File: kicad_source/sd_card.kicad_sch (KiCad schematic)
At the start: 7 parts, among them J1 Conn_01x08

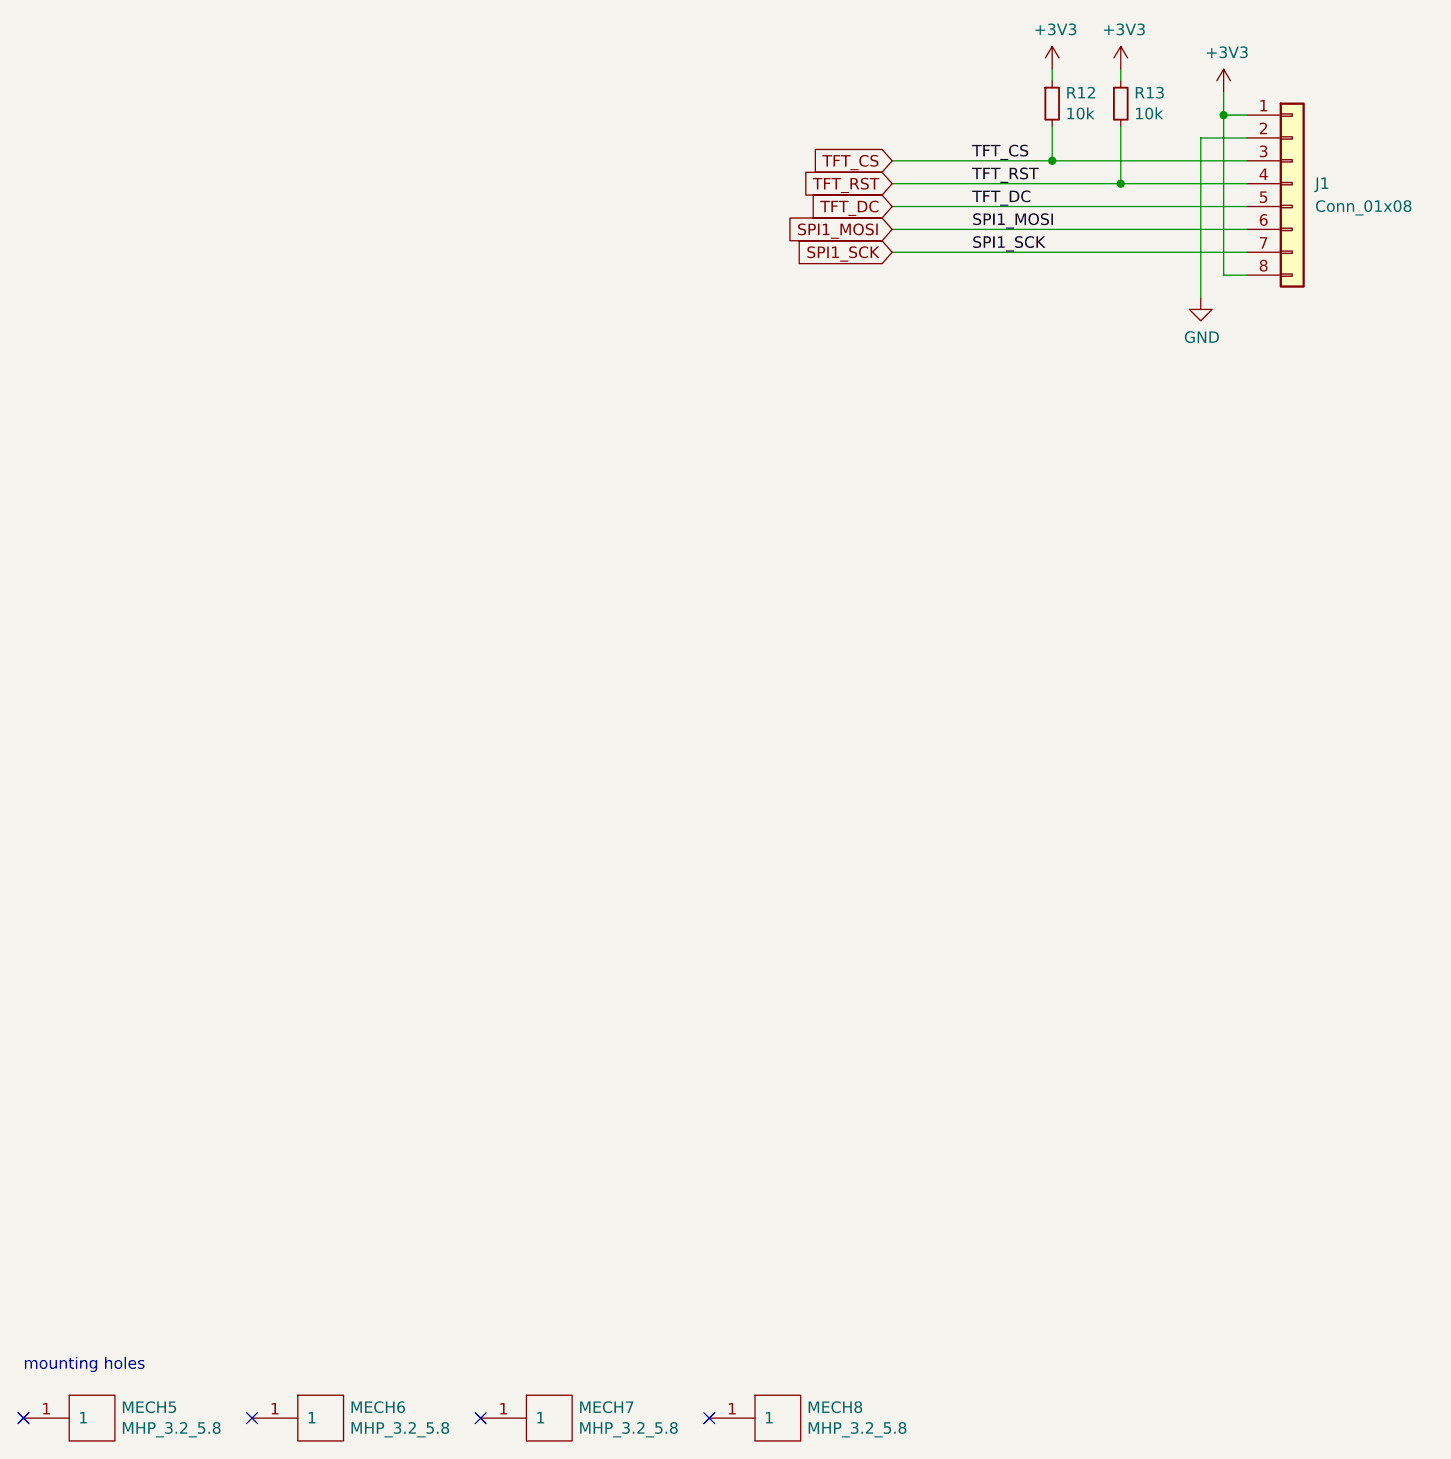
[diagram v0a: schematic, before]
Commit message: added sd card, updated layout
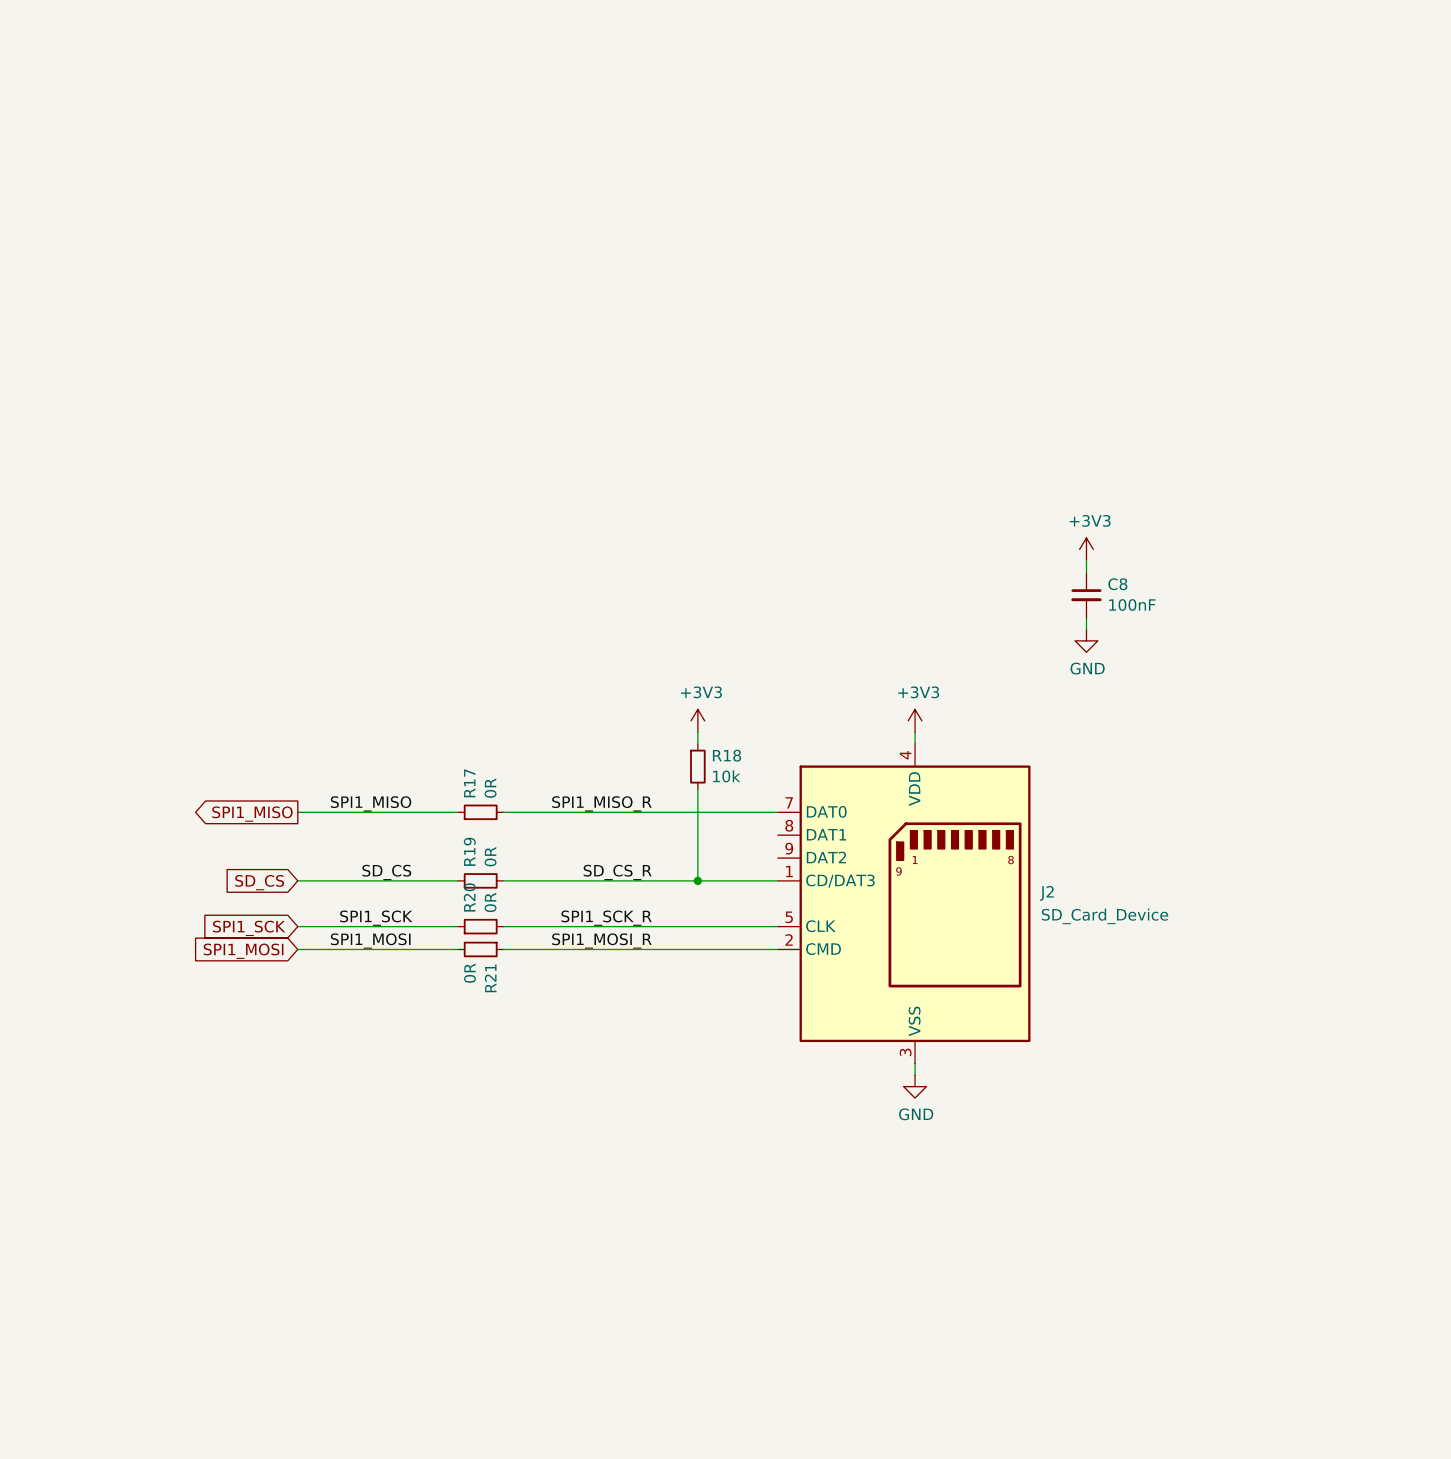
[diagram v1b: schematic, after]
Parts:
- removed J1: Conn_01x08, Connector_PinHeader_2.54mm:PinHeader_1x08_P2.54mm_Vertical, symbol Connector_Generic:Conn_01x08
- removed MECH5, MECH6, MECH7, MECH8: MHP_3.2_5.8, MountingHole:MountingHole_3.2mm_M3_ISO14580_Pad, symbol OpenCyphalPicoBase-rescue:MHP_3.2_5.8-MECH_mounting-holes
- removed R12, R13: 10k, Resistor_SMD:R_0603_1608Metric, symbol Device:R_Small
- added C8: 100nF, Capacitor_SMD:C_0603_1608Metric, symbol Device:C_Small
- added J2: SD_Card_Device, Connector_Card:microSD_HC_Molex_104031-0811, symbol Connector:SD_Card_Device
- added R17, R19, R20, R21: 0R, Resistor_SMD:R_0603_1608Metric, symbol Device:R_Small
- added R18: 10k, Resistor_SMD:R_0603_1608Metric, symbol Device:R_Small
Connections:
- net +3V3: now also C8.1, J2.4 (VDD), R18.1
- net GND: now also C8.2, J2.3 (VSS), J2.6 (VSS)
- net SPI1_MOSI: now also R21.2
- net SPI1_SCK: now also R20.1
- new net SD_CS: R19.1
- new net SD_CS_R: J2.1 (CD/DAT3), R18.2, R19.2
- new net SPI1_MISO: R17.1
- new net SPI1_MISO_R: J2.7 (DAT0), R17.2
- new net SPI1_MOSI_R: J2.2 (CMD), R21.1
- new net SPI1_SCK_R: J2.5 (CLK), R20.2
- no-connect marks 4 -> 0
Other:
- note removed: "mounting holes"

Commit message: added push button
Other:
- title: CyphalIMUBase/CAN -> CyphalHMIBase/CAN
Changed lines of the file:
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@@
 	(paper "A4")
 	(title_block
-		(title "CyphalIMUBase/CAN")
+		(title "CyphalHMIBase/CAN")
 		(date "2026-06-05")
 		(rev "0.1")
@@
 				(justify right)
 				(hide yes)
+			)
+		)
+	)
+	(symbol
+		(lib_id "OpenCyphalPicoBase-rescue:+3.3V-power-supply")
+		(at 133.35 111.76 0)
+		(unit 1)
+		(exclude_from_sim no)
+		(in_bom yes)
+		(on_board yes)
+		(dnp no)
+		(property "Reference" "#PWR53"
+			(at 133.35 115.57 0)
+			(effects
+				(font
+					(size 1.27 1.27)
+				)
+				(hide yes)
+			)
+		)
+		(property "Value" "+3V3"
+			(at 133.731 107.3658 0)
+			(effects
+				(font
+					(size 1.27 1.27)
+				)
+			)
+		)
+		(property "Footprint" ""
+			(at 133.35 111.76 0)
+			(effects
+				(font
+					(size 1.27 1.27)
+				)
+			)
+		)
+		(property "Datasheet" ""
+			(at 133.35 111.76 0)
+			(effects
+				(font
+					(size 1.27 1.27)
+				)
+			)
+		)
+		(property "Description" ""
+			(at 133.35 111.76 0)
+			(effects
+				(font
+					(size 1.27 1.27)
+				)
+				(hide yes)
+			)
+		)
+		(pin "1"
+		)
+		(instances
+			(project "CyphalHMIBase-CAN"
+				(path "/9d6d512e-1439-4aa2-b0d9-afb2dddd9146/e75f9fc4-b9ac-41b4-8a83-2ca859e56dc6"
+					(reference "#PWR53")
+					(unit 1)
+				)
 			)
 		)
@@
 	(symbol
 		(lib_id "OpenCyphalPicoBase-rescue:GND-power-supply")
+		(at 133.35 149.86 0)
+		(unit 1)
+		(exclude_from_sim no)
+		(in_bom yes)
+		(on_board yes)
+		(dnp no)
+		(property "Reference" "#PWR55"
+			(at 133.35 156.21 0)
+			(effects
+				(font
+					(size 1.27 1.27)
+				)
+				(hide yes)
+			)
+		)
+		(property "Value" "GND"
+			(at 133.477 154.2542 0)
+			(effects
+				(font
+					(size 1.27 1.27)
+				)
+			)
+		)
+		(property "Footprint" ""
+			(at 133.35 149.86 0)
+			(effects
+				(font
+					(size 1.27 1.27)
+				)
+			)
+		)
+		(property "Datasheet" ""
+			(at 133.35 149.86 0)
+			(effects
+				(font
+					(size 1.27 1.27)
+				)
+			)
+		)
+		(property "Description" ""
+			(at 133.35 149.86 0)
+			(effects
+				(font
+					(size 1.27 1.27)
+				)
+				(hide yes)
+			)
+		)
+		(pin "1"
+		)
+		(instances
+			(project "CyphalHMIBase-CAN"
+				(path "/9d6d512e-1439-4aa2-b0d9-afb2dddd9146/e75f9fc4-b9ac-41b4-8a83-2ca859e56dc6"
+					(reference "#PWR55")
+					(unit 1)
+				)
+			)
+		)
+	)
+	(symbol
+		(lib_id "OpenCyphalPicoBase-rescue:GND-power-supply")
 		(at 152.4 100.33 0)
 		(unit 1)
@@
 	(symbol
 		(lib_id "Device:R_Small")
+		(at 85.09 128.27 90)
+		(unit 1)
+		(exclude_from_sim no)
+		(in_bom yes)
+		(on_board yes)
+		(dnp no)
+		(property "Reference" "R19"
+			(at 83.9216 126.7714 0)
+			(effects
+				(font
+					(size 1.27 1.27)
+				)
+				(justify left)
+			)
+		)
+		(property "Value" "0R"
+			(at 86.233 126.7714 0)
+			(effects
+				(font
+					(size 1.27 1.27)
+				)
+				(justify left)
+			)
+		)
+		(property "Footprint" "Resistor_SMD:R_0603_1608Metric"
+			(at 88.9 128.27 0)
+			(effects
+				(font
+					(size 1.27 1.27)
+				)
+				(hide yes)
+			)
+		)
+		(property "Datasheet" ""
+			(at 85.09 128.27 0)
+			(effects
+				(font
+					(size 1.27 1.27)
+				)
+			)
+		)
+		(property "Description" ""
+			(at 85.09 128.27 0)
+			(effects
+				(font
+					(size 1.27 1.27)
+				)
+				(hide yes)
+			)
+		)
+		(property "LCSC" "C22775"
+			(at 85.09 128.27 0)
+			(effects
+				(font
+					(size 1.27 1.27)
+				)
+				(hide yes)
+			)
+		)
+		(pin "1"
+		)
+		(pin "2"
+		)
+		(instances
+			(project "CyphalHMIBase-CAN"
+				(path "/9d6d512e-1439-4aa2-b0d9-afb2dddd9146/e75f9fc4-b9ac-41b4-8a83-2ca859e56dc6"
+					(reference "R19")
+					(unit 1)
+				)
+			)
+		)
+	)
+	(symbol
+		(lib_id "Device:R_Small")
 		(at 109.22 115.57 0)
 		(unit 1)
@@
 				(path "/9d6d512e-1439-4aa2-b0d9-afb2dddd9146/e75f9fc4-b9ac-41b4-8a83-2ca859e56dc6"
 					(reference "R18")
-					(unit 1)
-				)
-			)
-		)
-	)
-	(symbol
-		(lib_id "Device:R_Small")
-		(at 85.09 128.27 90)
-		(unit 1)
-		(exclude_from_sim no)
-		(in_bom yes)
-		(on_board yes)
-		(dnp no)
-		(property "Reference" "R19"
-			(at 83.9216 126.7714 0)
-			(effects
-				(font
-					(size 1.27 1.27)
-				)
-				(justify left)
-			)
-		)
-		(property "Value" "0R"
-			(at 86.233 126.7714 0)
-			(effects
-				(font
-					(size 1.27 1.27)
-				)
-				(justify left)
-			)
-		)
-		(property "Footprint" "Resistor_SMD:R_0603_1608Metric"
-			(at 88.9 128.27 0)
-			(effects
-				(font
-					(size 1.27 1.27)
-				)
-				(hide yes)
-			)
-		)
-		(property "Datasheet" ""
-			(at 85.09 128.27 0)
-			(effects
-				(font
-					(size 1.27 1.27)
-				)
-			)
-		)
-		(property "Description" ""
-			(at 85.09 128.27 0)
-			(effects
-				(font
-					(size 1.27 1.27)
-				)
-				(hide yes)
-			)
-		)
-		(property "LCSC" "C22775"
-			(at 85.09 128.27 0)
-			(effects
-				(font
-					(size 1.27 1.27)
-				)
-				(hide yes)
-			)
-		)
-		(pin "1"
-		)
-		(pin "2"
-		)
-		(instances
-			(project "CyphalHMIBase-CAN"
-				(path "/9d6d512e-1439-4aa2-b0d9-afb2dddd9146/e75f9fc4-b9ac-41b4-8a83-2ca859e56dc6"
-					(reference "R19")
 					(unit 1)
 				)
@@
 					(unit 1)
 				)
-			)
-		)
-	)
-	(symbol
-		(lib_id "OpenCyphalPicoBase-rescue:+3.3V-power-supply")
-		(at 133.35 111.76 0)
-		(unit 1)
-		(exclude_from_sim no)
-		(in_bom yes)
-		(on_board yes)
-		(dnp no)
-		(property "Reference" "#PWR53"
-			(at 133.35 115.57 0)
-			(effects
-				(font
-					(size 1.27 1.27)
-				)
-				(hide yes)
-			)
-		)
-		(property "Value" "+3V3"
-			(at 133.731 107.3658 0)
-			(effects
-				(font
-					(size 1.27 1.27)
-				)
-			)
-		)
-		(property "Footprint" ""
-			(at 133.35 111.76 0)
-			(effects
-				(font
-					(size 1.27 1.27)
-				)
-			)
-		)
-		(property "Datasheet" ""
-			(at 133.35 111.76 0)
-			(effects
-				(font
-					(size 1.27 1.27)
-				)
-			)
-		)
-		(property "Description" ""
-			(at 133.35 111.76 0)
-			(effects
-				(font
-					(size 1.27 1.27)
-				)
-				(hide yes)
-			)
-		)
-		(pin "1"
-		)
-		(instances
-			(project "CyphalHMIBase-CAN"
-				(path "/9d6d512e-1439-4aa2-b0d9-afb2dddd9146/e75f9fc4-b9ac-41b4-8a83-2ca859e56dc6"
-					(reference "#PWR53")
-					(unit 1)
-				)
-			)
-		)
-	)
-	(symbol
-		(lib_id "OpenCyphalPicoBase-rescue:GND-power-supply")
-		(at 133.35 149.86 0)
-		(unit 1)
-		(exclude_from_sim no)
-		(in_bom yes)
-		(on_board yes)
-		(dnp no)
-		(property "Reference" "#PWR55"
-			(at 133.35 156.21 0)
-			(effects
-				(font
-					(size 1.27 1.27)
-				)
-				(hide yes)
-			)
-		)
-		(property "Value" "GND"
-			(at 133.477 154.2542 0)
-			(effects
-				(font
-					(size 1.27 1.27)
-				)
-			)
-		)
-		(property "Footprint" ""
-			(at 133.35 149.86 0)
-			(effects
-				(font
-					(size 1.27 1.27)
-				)
-			)
-		)
-		(property "Datasheet" ""
-			(at 133.35 149.86 0)
-			(effects
-				(font
-					(size 1.27 1.27)
-				)
-			)
-		)
-		(property "Description" ""
-			(at 133.35 149.86 0)
-			(effects
-				(font
-					(size 1.27 1.27)
-				)
-				(hide yes)
-			)
-		)
-		(pin "1"
-		)
-		(instances
-			(project "CyphalHMIBase-CAN"
-				(path "/9d6d512e-1439-4aa2-b0d9-afb2dddd9146/e75f9fc4-b9ac-41b4-8a83-2ca859e56dc6"
-					(reference "#PWR55")
-					(unit 1)
-				)

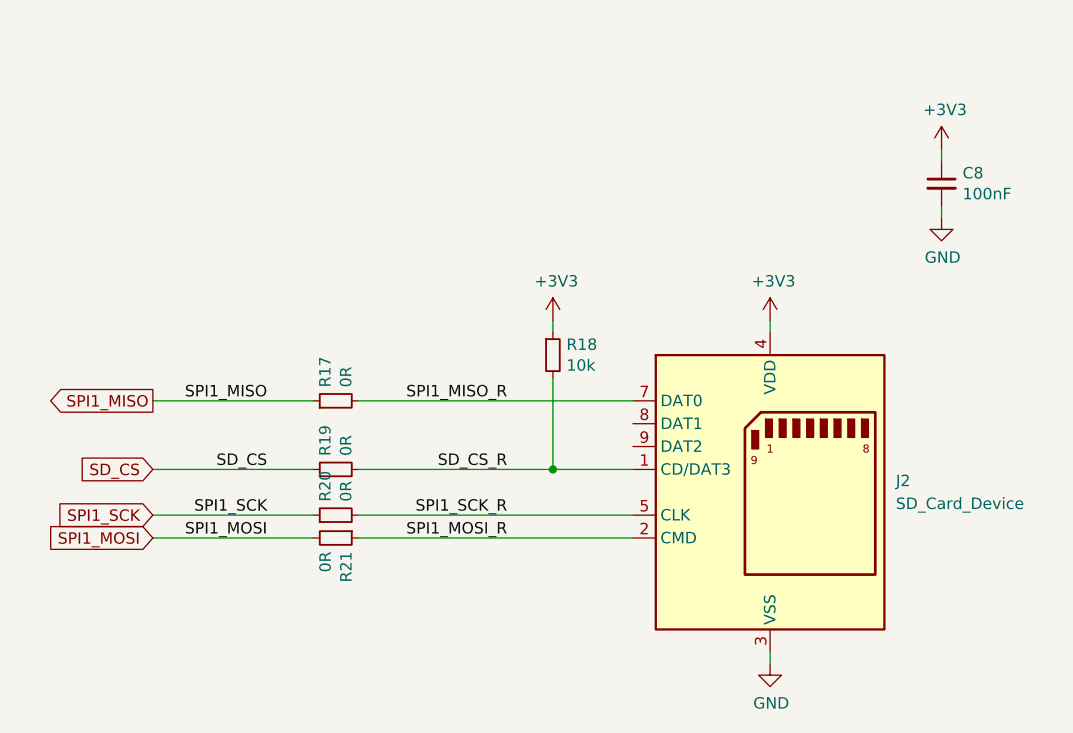
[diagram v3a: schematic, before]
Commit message: fixed micro sd card connector
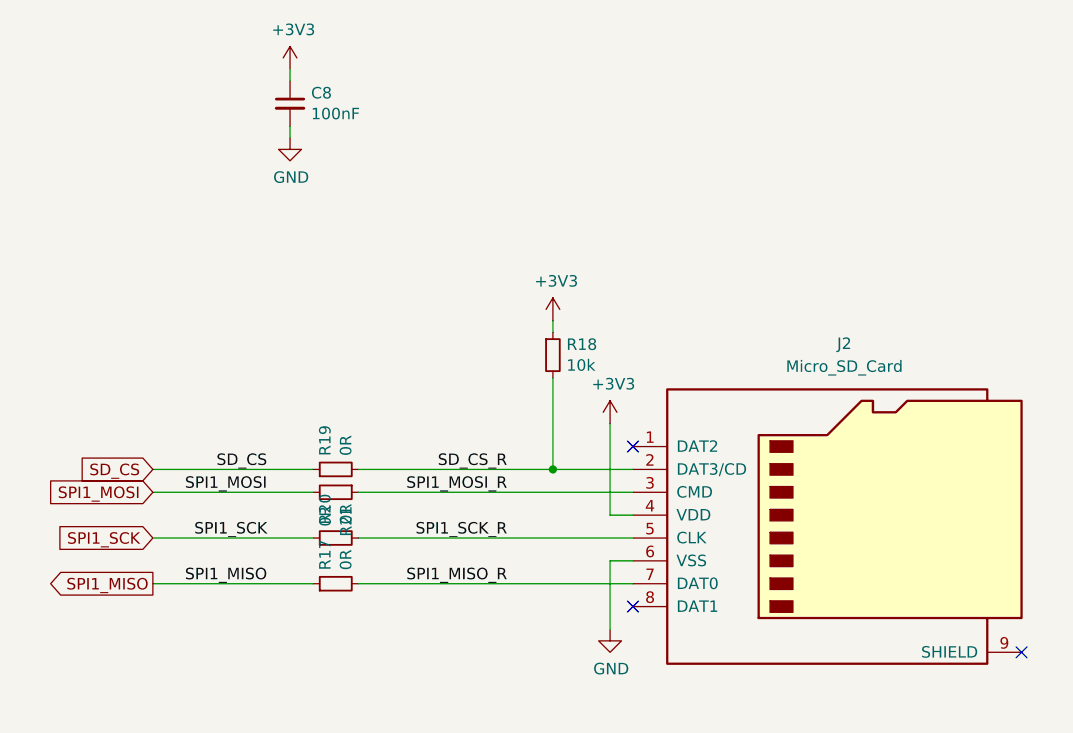
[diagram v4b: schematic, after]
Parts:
- removed J2: SD_Card_Device, Connector_Card:microSD_HC_Molex_104031-0811, symbol Connector:SD_Card_Device
- added J2: Micro_SD_Card, generationmake:WE_693071010811, symbol Connector:Micro_SD_Card
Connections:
- net +3V3: now also J2.4 (VDD)
- net GND: now also J2.6 (VSS)
- net SD_CS_R: now also J2.2 (DAT3/CD)
- net SPI1_MISO_R: now also J2.7 (DAT0)
- net SPI1_MOSI_R: now also J2.3 (CMD)
- net SPI1_SCK_R: now also J2.5 (CLK)
- no-connect marks 0 -> 3
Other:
- moved on the sheet: C8, R17, R20, R21
